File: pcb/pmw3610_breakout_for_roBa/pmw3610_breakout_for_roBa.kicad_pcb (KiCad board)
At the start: 2 copper layers, 22 x 23.5 mm, 13 parts, among them J2 vik-module-connector, U1 MCP1700T-1802E/TT, U2 PMW3610

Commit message: Update pmw3610 breakout
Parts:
- moved C7 20.5 mm to (145.2, 92.6)
- moved C2 18.1 mm to (145.2, 89.1)
- moved C4 17.9 mm to (127.0, 96.8), turned to 180 degrees
- moved C6 9.84 mm to (145.2, 94.5), turned to 0 degrees
- moved C9 7.29 mm to (145.1, 83.5)
- moved C1 5.13 mm to (145.2, 90.7)
- moved R1 3.67 mm to (126.7, 87.5), turned to 0 degrees
- moved C5 2.46 mm to (145.8, 86.4)
- moved C3 2.22 mm to (126.7, 89.9), turned to 180 degrees
- moved C8 0.92 mm to (145.1, 81.5)
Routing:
- net GND: track 68.6 -> 15.1 mm, vias 3 -> 5
- net Net-(U2-VCP): track 49.8 -> 5.01 mm, vias 6 -> 0
- net +1V9: track 68.4 -> 25.7 mm, vias 12 -> 2
- net Net-(U2-+VCSEL): track 52.3 -> 41.2 mm, vias 1 -> 3
- net MOTION: track 21.1 -> 12.7 mm, vias 2 -> 3
- net Net-(U2-NRESET): track 3.49 -> 8.60 mm
- net SCLK: track 23.2 -> 27.1 mm, vias 0 -> 3
- net Net-(U2-CP): track 2.60 -> 5.28 mm
- net Net-(U2-CN): track 2.64 -> 5.16 mm
- net NCS: track 26.9 -> 24.5 mm, vias 2 -> 4
- net SDIO: track 27.5 -> 25.7 mm, vias 2 -> 1
- net VCC: track 39.4 -> 40.6 mm
- added copper zone on B.Cu, net GND
- added copper zone on F.Cu, net GND

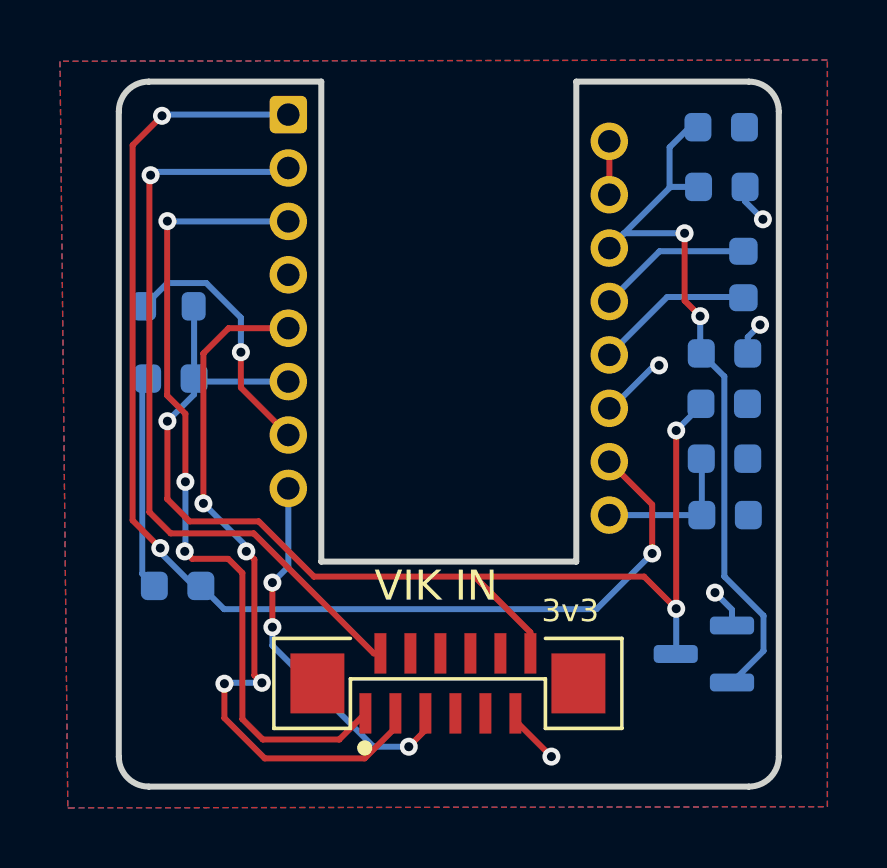
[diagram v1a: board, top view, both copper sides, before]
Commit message: Change C1 value according to datasheet
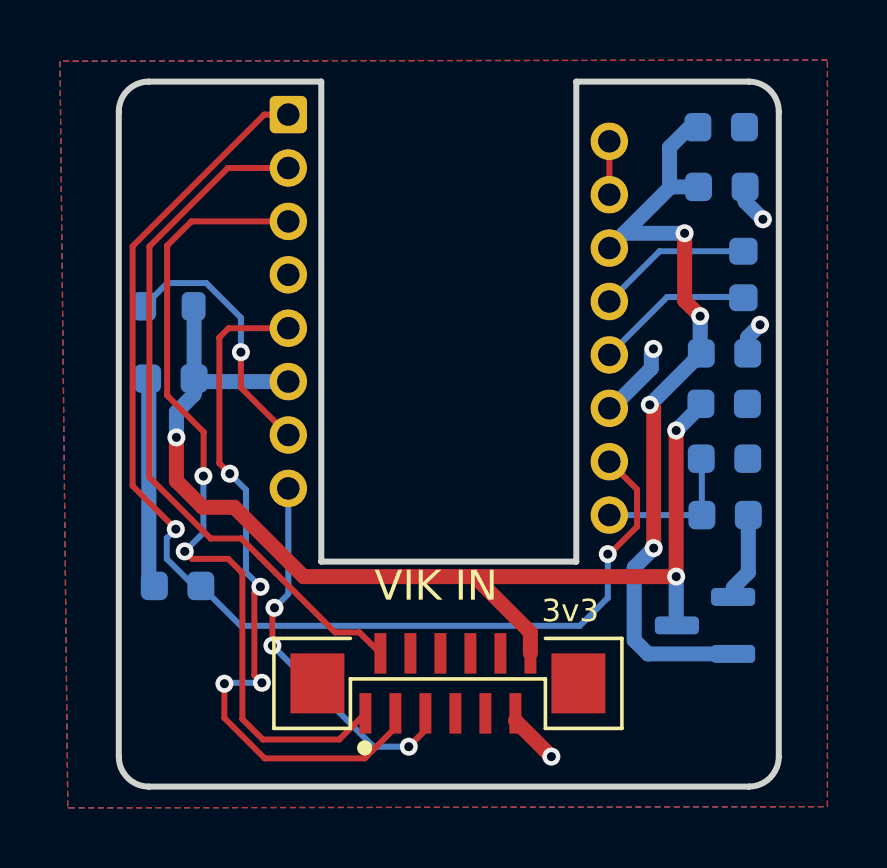
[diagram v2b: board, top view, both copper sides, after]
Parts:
- moved U1 0.95 mm to (144.5, 98.1)
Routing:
- net VCC: track 40.6 -> 38.4 mm
- net SDIO: track 25.7 -> 23.5 mm, vias 1 -> 0
- net GND: track 15.1 -> 17.0 mm, vias 5 -> 4
- net +1V9: track 25.7 -> 27.5 mm, vias 2 -> 4
- net Net-(U2-+VCSEL): track 41.2 -> 39.5 mm, vias 3 -> 2
- net SCLK: track 27.1 -> 27.2 mm, vias 3 -> 2

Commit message: Fix capacitor values and generate production files
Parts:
- C1, C2: value 1u -> 1uF
- C3, C8: value 100n -> 100nF
- C4: value 10n -> 10nF
- C5: value 100n (X7R) -> 100nF (X7R)
- C6: value 10u (X7R) -> 10uF (X7R)
- C7: value 10n (X7R) -> 10nF (X7R)
- C9: value 3.3u/25V -> 3.3uF/16V
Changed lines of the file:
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@@
 			)
 		)
-		(property "Value" "1u"
+		(property "Value" "1uF"
 			(at 0 -1.43 0)
 			(layer "B.Fab")
@@
 		)
 		(property "LCSC" "C15849"
-			(at 0 0 180)
-			(unlocked yes)
-			(layer "B.Fab")
-			(hide yes)
-			(effects
-				(font
-					(size 1 1)
-					(thickness 0.15)
-				)
-				(justify mirror)
+			(at 0 0 0)
+			(layer "B.SilkS")
+			(hide yes)
+			(effects
+				(font
+					(size 1.27 1.27)
+					(thickness 0.15)
+				)
 			)
 		)
@@
 			)
 		)
-		(property "Value" "10n (X7R)"
+		(property "Value" "10nF (X7R)"
 			(at 0 -1.43 0)
 			(layer "B.Fab")
@@
 			)
 		)
-		(property "LCSC" "C19666"
-			(at 0 0 180)
-			(unlocked yes)
-			(layer "B.Fab")
-			(hide yes)
-			(effects
-				(font
-					(size 1 1)
-					(thickness 0.15)
-				)
-				(justify mirror)
+		(property "LCSC" "C57112"
+			(at 0 0 0)
+			(layer "B.SilkS")
+			(hide yes)
+			(effects
+				(font
+					(size 1.27 1.27)
+					(thickness 0.15)
+				)
 			)
 		)
@@
 			)
 		)
-		(property "Value" "100n (X7R)"
+		(property "Value" "100nF (X7R)"
 			(at 0 -1.43 90)
 			(layer "B.Fab")
@@
 			)
 		)
-		(property "LCSC" "C19666"
-			(at 0 0 90)
-			(unlocked yes)
-			(layer "B.Fab")
-			(hide yes)
-			(effects
-				(font
-					(size 1 1)
-					(thickness 0.15)
-				)
-				(justify mirror)
+		(property "LCSC" "C14663"
+			(at 0 0 0)
+			(layer "B.SilkS")
+			(hide yes)
+			(effects
+				(font
+					(size 1.27 1.27)
+					(thickness 0.15)
+				)
 			)
 		)
@@
 			)
 		)
-		(property "Value" "1u"
+		(property "Value" "1uF"
 			(at 0 -1.43 180)
 			(layer "B.Fab")
@@
 			)
 		)
-		(property "LCSC" "C14663"
-			(at 0 0 0)
-			(unlocked yes)
-			(layer "B.Fab")
-			(hide yes)
-			(effects
-				(font
-					(size 1 1)
-					(thickness 0.15)
-				)
-				(justify mirror)
+		(property "LCSC" "C15849"
+			(at 0 0 0)
+			(layer "B.SilkS")
+			(hide yes)
+			(effects
+				(font
+					(size 1.27 1.27)
+					(thickness 0.15)
+				)
 			)
 		)
@@
 			)
 		)
-		(property "Value" "3.3u/25V"
+		(property "Value" "3.3uF/16V"
 			(at 0 -1.43 0)
 			(layer "B.Fab")
@@
 			)
 		)
-		(property "LCSC" "C19666"
-			(at 0 0 180)
-			(unlocked yes)
-			(layer "B.Fab")
-			(hide yes)
-			(effects
-				(font
-					(size 1 1)
-					(thickness 0.15)
-				)
-				(justify mirror)
+		(property "LCSC" "C51412"
+			(at 0 0 0)
+			(layer "B.SilkS")
+			(hide yes)
+			(effects
+				(font
+					(size 1.27 1.27)
+					(thickness 0.15)
+				)
 			)
 		)
@@
 			)
 		)
-		(property "Value" "100n"
+		(property "Value" "100nF"
 			(at 0 -1.43 0)
 			(layer "B.Fab")
@@
 			)
 		)
-		(property "LCSC" "C19666"
-			(at 0 0 180)
-			(unlocked yes)
-			(layer "B.Fab")
-			(hide yes)
-			(effects
-				(font
-					(size 1 1)
-					(thickness 0.15)
-				)
-				(justify mirror)
+		(property "LCSC" "C14663"
+			(at 0 0 0)
+			(layer "B.SilkS")
+			(hide yes)
+			(effects
+				(font
+					(size 1.27 1.27)
+					(thickness 0.15)
+				)
 			)
 		)
@@
 			)
 		)
-		(property "Value" "10u (X7R)"
+		(property "Value" "10uF (X7R)"
 			(at 0 -1.43 0)
 			(layer "B.Fab")
@@
 			)
 		)
-		(property "LCSC" "C19666"
-			(at 0 0 180)
-			(unlocked yes)
-			(layer "B.Fab")
-			(hide yes)
-			(effects
-				(font
-					(size 1 1)
-					(thickness 0.15)
-				)
-				(justify mirror)
+		(property "LCSC" "C2959727"
+			(at 0 0 0)
+			(layer "B.SilkS")
+			(hide yes)
+			(effects
+				(font
+					(size 1.27 1.27)
+					(thickness 0.15)
+				)
 			)
 		)
@@
 			)
 		)
-		(property "Value" "10n"
+		(property "Value" "10nF"
 			(at 0 -1.43 0)
 			(layer "B.Fab")
@@
 			)
 		)
-		(property "LCSC" "C19666"
-			(at 0 0 0)
-			(unlocked yes)
-			(layer "B.Fab")
-			(hide yes)
-			(effects
-				(font
-					(size 1 1)
-					(thickness 0.15)
-				)
-				(justify mirror)
+		(property "LCSC" "C57112"
+			(at 0 0 0)
+			(layer "B.SilkS")
+			(hide yes)
+			(effects
+				(font
+					(size 1.27 1.27)
+					(thickness 0.15)
+				)
 			)
 		)
@@
 			)
 		)
-		(property "Value" "100n"
+		(property "Value" "100nF"
 			(at 0 -1.44 0)
 			(layer "B.Fab")
@@
 			)
 		)
-		(property "LCSC" "C19666"
-			(at 0 0 0)
-			(unlocked yes)
-			(layer "B.Fab")
-			(hide yes)
-			(effects
-				(font
-					(size 1 1)
-					(thickness 0.15)
-				)
-				(justify mirror)
+		(property "LCSC" "C14663"
+			(at 0 0 0)
+			(layer "B.SilkS")
+			(hide yes)
+			(effects
+				(font
+					(size 1.27 1.27)
+					(thickness 0.15)
+				)
 			)
 		)
@@
 			)
 		)
+		(property "LCSC" "C22976"
+			(at 0 0 0)
+			(layer "B.SilkS")
+			(hide yes)
+			(effects
+				(font
+					(size 1.27 1.27)
+					(thickness 0.15)
+				)
+			)
+		)
